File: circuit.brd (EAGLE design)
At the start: 63.2 x 40.6 mm, 13 parts, among them IC1 LM324N, IC2 LM324N

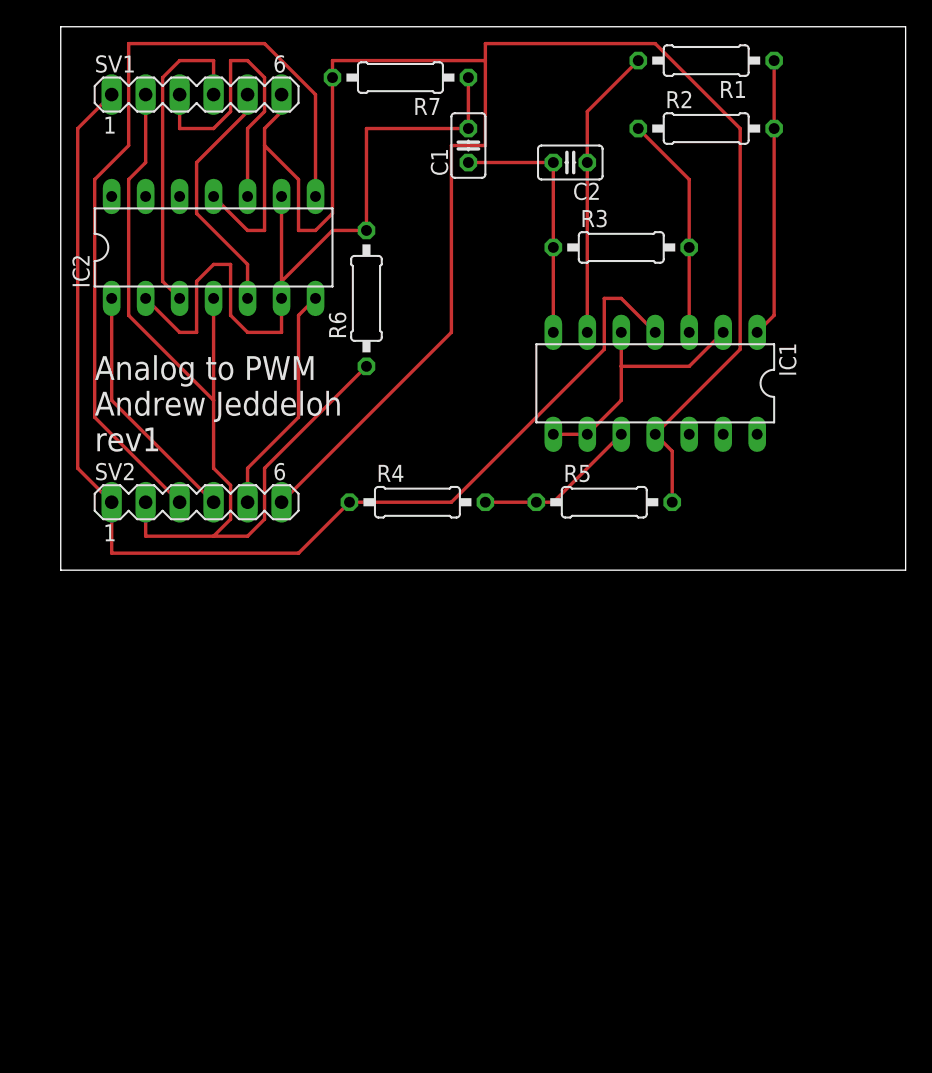
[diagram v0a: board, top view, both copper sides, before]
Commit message: Updated to use comparator instead of op amps
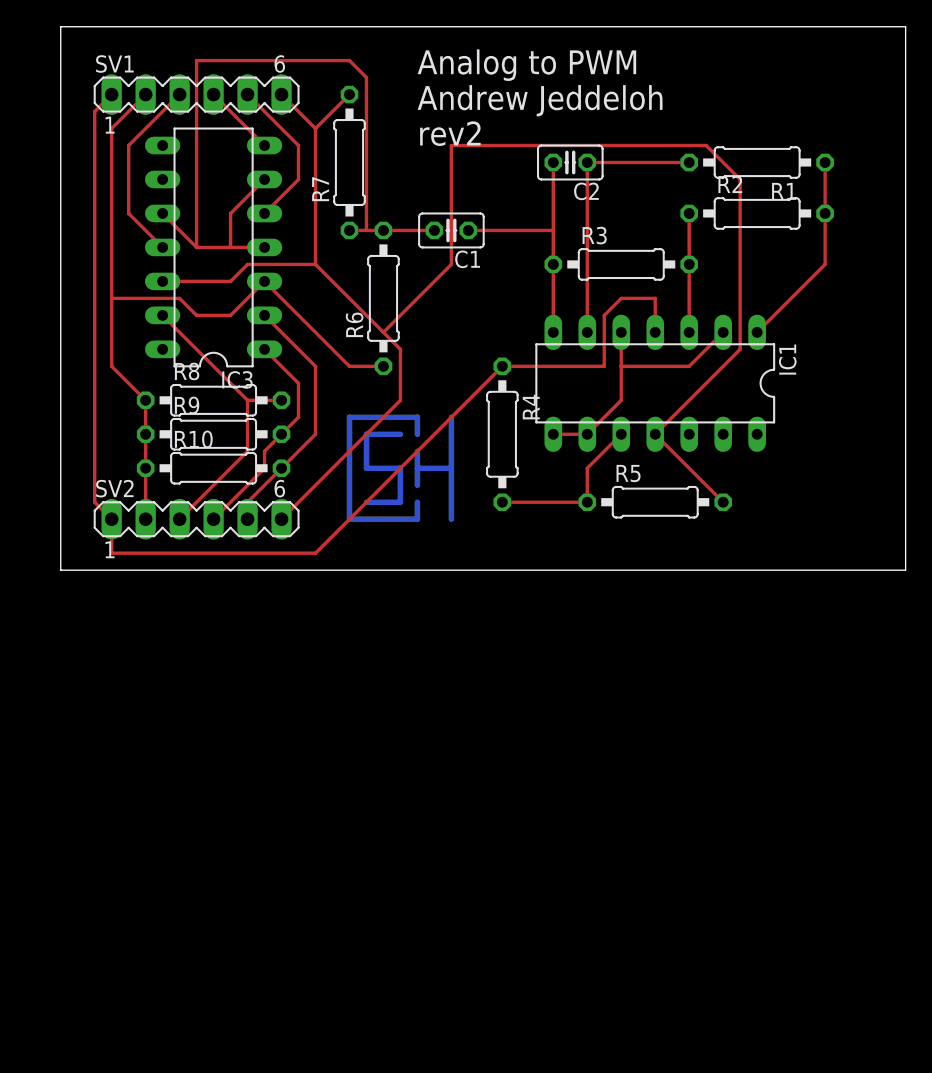
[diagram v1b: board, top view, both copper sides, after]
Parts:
- added R10, R8, R9: 10k, rcl:0207/10
- IC3: value LM324N -> LM339N
- moved R1 8.52 mm to (54.6, 66.0)
- moved R4 8.13 mm to (35.6, 45.7), turned to 270 degrees
- moved R2 7.41 mm to (54.6, 62.2)
- moved R7 7.41 mm to (24.1, 66.0), turned to 90 degrees
- moved C1 6.48 mm to (31.8, 61.0), turned to 180 degrees
- moved R5 3.81 mm to (47.0, 40.6)
- moved R6 1.27 mm to (26.7, 55.9)
- moved SV2 1.27 mm to (12.7, 39.4)
- moved R3 1.27 mm to (44.5, 58.4)
- turned IC3 to 90 degrees
- renumbered IC2 to IC3
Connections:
- net +5V: now also IC3.3, R10.1, R8.1, R9.1; no longer IC3.4
- net GND: now also IC3.12; no longer IC3.11
- net N$10: now also IC3.13, R8.2; no longer IC3.8
- net N$11: now also R9.2
- net N$12: now also IC3.2, R10.2; no longer IC3.7
- net N$13: now also IC3.11; no longer IC3.10
- net N$14: now also IC3.7; no longer IC3.3
- net N$6: now also IC3.10, IC3.4; no longer IC3.2, IC3.9
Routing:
- net N$10: track 61.1 -> 22.5 mm
- net GND: track 143.7 -> 122.2 mm
- net N$5: track 0.00 -> 20.3 mm
- net N$14: track 23.9 -> 5.39 mm
- net +5V: track 71.4 -> 58.4 mm
- net N$16: track 0.00 -> 12.7 mm
- net N$7: track 0.00 -> 12.7 mm
- net N$13: track 23.2 -> 14.1 mm
- net N$9: track 16.8 -> 8.89 mm
- net N$15: track 18.4 -> 11.5 mm
- net N$3: track 20.8 -> 14.8 mm
- net N$6: track 57.0 -> 59.8 mm
- net N$11: track 18.4 -> 16.4 mm
- net N$12: track 17.3 -> 18.9 mm
- net N$4: track 21.9 -> 20.3 mm
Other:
- board text added: "Analog to PWM Andrew Jeddeloh rev2"
- board text removed: "Analog to PWM Andrew Jeddeloh rev1"

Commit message: schematic: added decoupling caps for each IC as well as zener diodes so that the amplitude of the triangle wave is not dependent on supply voltage. Also added a trimpot to allow for triangle wave adjustment. board: redid board with ground plane
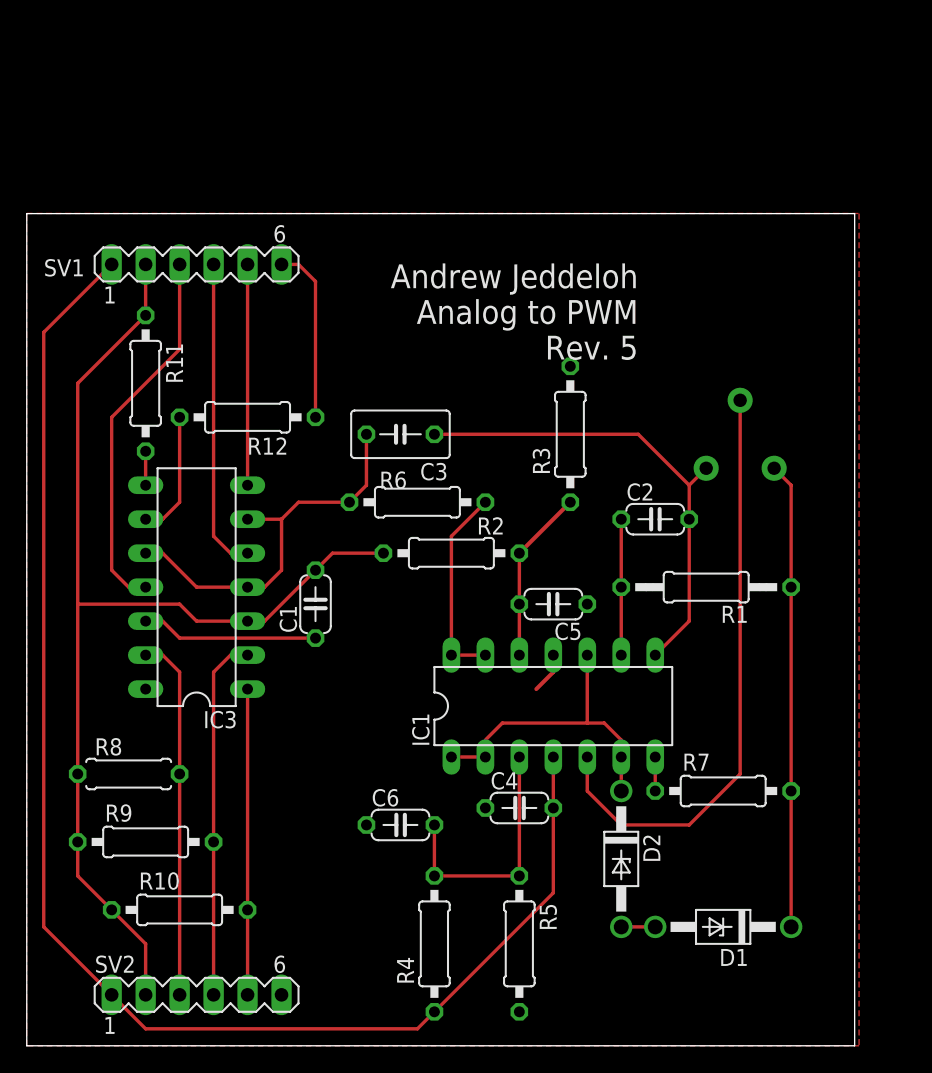
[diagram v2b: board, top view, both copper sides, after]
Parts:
- added ADJ: 10k, SparkFun-Electromechanical:TRIM_POT
- added C3: 1uF, resistor:C050-035X075
- added C4, C5, C6: 100nf, rcl:C050-024X044
- added D1, D2: 3.9v, diode:DO41Z10
- added R11, R12: 10k, rcl:0207/10
- C1, C2: device rcl:C025-025X050 -> rcl:C050-024X044
- R1: device rcl:0207/10 -> rcl:0207/12
- R2: value 20k -> 10k
- R3: value 8.3k -> 10k
- R6: value 1M -> 10k
- R7: value 1M -> 100
- R8: device rcl:0207/10 -> rcl:0207/7
- moved R7 54.7 mm to (52.1, 19.1), turned to 0 degrees
- moved R4 38.4 mm to (30.5, 7.62), turned to 90 degrees
- moved SV2 35.6 mm to (12.7, 3.81)
- moved R5 34.5 mm to (36.8, 7.62), turned to 270 degrees
- moved R2 34.2 mm to (31.8, 36.8)
- moved R10 33.1 mm to (11.4, 10.2)
- moved R1 32.0 mm to (50.8, 34.3)
- moved R9 30.9 mm to (8.89, 15.2)
- moved C1 29.7 mm to (21.6, 33.0), turned to 90 degrees
- moved R8 28.7 mm to (7.62, 20.3)
- moved C2 27.4 mm to (47.0, 39.4), turned to 0 degrees
- moved IC3 25.4 mm to (12.7, 34.3)
- moved IC1 25.3 mm to (39.4, 25.4), turned to 0 degrees
- moved R6 15.5 mm to (29.2, 40.6), turned to 180 degrees
- moved R3 13.3 mm to (40.6, 45.7), turned to 90 degrees
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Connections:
- removed net N$6: C1.2, IC3.10, IC3.4, IC3.6, R6.2, R7.1
- new net ARTGND: D2.C, IC1.1, IC1.10, IC1.2, IC1.6
- new net N$16: C5.2, IC1.12, R2.2, R3.1
- new net N$17: IC3.8, R11.2
- new net N$18: IC3.9, R12.2
- new net N$19: C3.2, IC3.10, IC3.4, IC3.6, R6.2
- new net N$5: IC1.13, IC1.14, R6.1
- new net N$7: ADJ.3, D1.C, R1.1, R7.2
- net +5V: now also C1.2, R11.1, R2.1; no longer R6.1
- net GND: now also C1.1, C4.1, C5.1, C6.1, R12.1, R3.2; no longer R7.2
- net N$1: now also ADJ.2, C3.1, IC1.8; no longer C1.1, IC1.7, R3.1
- net N$11: now also IC3.2; no longer IC3.1
- net N$12: now also IC3.1; no longer IC3.2
- net N$14: now also IC3.5; no longer IC3.7
- net N$15: now also IC3.7; no longer IC3.5
- net N$2: now also IC1.7, R7.1; no longer IC1.2, IC1.5, IC1.8, IC1.9
- net N$3: now also D1.A, D2.A; no longer IC1.1, R1.1, R2.2
- net N$4: now also IC1.9; no longer IC1.6
- net N$8: now also C6.2, IC1.3; no longer IC1.10
- net N$9: now also ADJ.1, IC1.5; no longer IC1.3, R2.1, R3.2
- net VCC: now also C4.2
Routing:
- net GND: track 122.2 -> 29.5 mm
- net N$6: track 59.8 -> 0.00 mm
- net N$9: track 8.89 -> 44.5 mm
- net N$19: track 0.00 -> 29.3 mm
- net +5V: track 58.4 -> 84.3 mm
- net ARTGND: track 0.00 -> 22.6 mm
- net N$7: track 12.7 -> 34.8 mm
- net VCC: track 88.6 -> 107.3 mm
- net N$14: track 5.39 -> 23.4 mm
- net N$2: track 19.9 -> 2.54 mm
- net N$1: track 19.0 -> 36.2 mm
- net N$13: track 14.1 -> 28.0 mm
- net N$3: track 14.8 -> 2.54 mm
- net N$11: track 16.4 -> 27.2 mm
- net N$4: track 20.3 -> 10.2 mm
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- added copper zone on layer 1, net GND
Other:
- board size 63.2 x 40.6 mm -> 61.9 x 62.2 mm
- board text added: "Andrew Jeddeloh Analog to PWM Rev. 5"
- board text removed: "Analog to PWM Andrew Jeddeloh rev2"
